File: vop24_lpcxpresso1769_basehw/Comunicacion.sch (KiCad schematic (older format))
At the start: 27 parts, among them J301 USB_B_Micro, J302 Conn_01x06_Male, J303 Conn_01x05_Male, J304 Screw_Terminal_01x02, U301 TPD4S014, U302 LTC4411, U303 LT1512

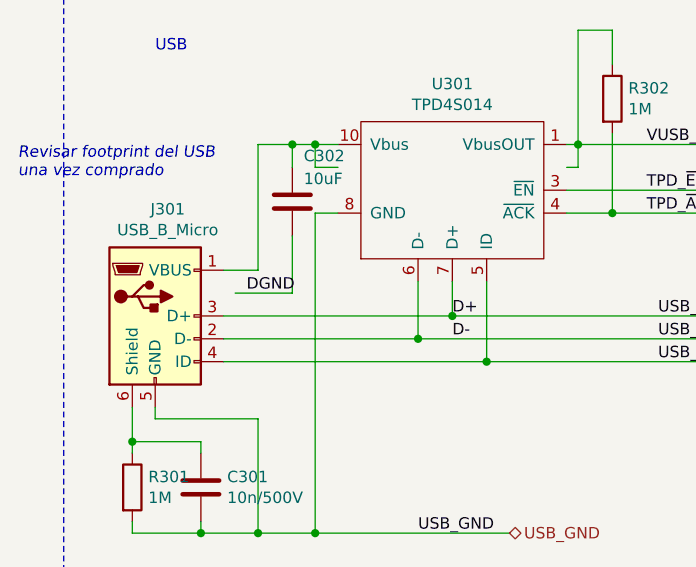
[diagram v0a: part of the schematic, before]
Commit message: PCB: ruteo e ubicacion de USB.    ESQ: cambios de etiquetas de gnd en usb
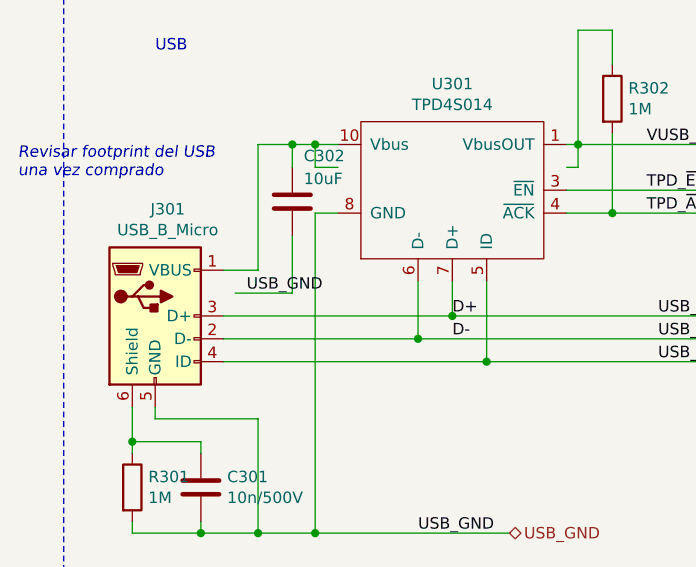
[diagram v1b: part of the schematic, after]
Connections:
- net labels removed: DGND
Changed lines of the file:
@@
 Wire Wire Line
 	1400 3800 2400 3800
-$Comp
-L vop24_lpcxpresso1769_basehw-rescue:USB_B_Micro-Connector J301
-U 1 1 5BAE3529
-P 1100 3800
-AR Path="/5BAE3529" Ref="J301"  Part="1"
-AR Path="/5B9DAB38/5BAE3529" Ref="J301"  Part="1"
-F 0 "J301" H 1155 4267 50  0000 C CNN
-F 1 "USB_B_Micro" H 1155 4176 50  0000 C CNN
-F 2 "Connector_USB:USB_Mini-B_Lumberg_2486_01_Horizontal" H 1250 3750 50  0001 C CNN
-F 3 "~" H 1250 3750 50  0001 C CNN
-	1    1100 3800
-	1    0    0    -1
-$EndComp
 Wire Wire Line
 	1400 4000 2550 4000
@@
 Wire Wire Line
 	1700 3450 1700 3700
-Text Label 1500 3700 0    50   ~ 0
-DGND
 Text Notes 500  3200 0    50   Italic 0
 Revisar footprint del USB \nuna vez comprado
@@
 Wire Wire Line
 	2950 3150 2950 3050
+$Comp
+L vop24_lpcxpresso1769_basehw-rescue:USB_B_Micro-Connector J301
+U 1 1 5BAE3529
+P 1100 3800
+AR Path="/5BAE3529" Ref="J301"  Part="1"
+AR Path="/5B9DAB38/5BAE3529" Ref="J301"  Part="1"
+F 0 "J301" H 1155 4267 50  0000 C CNN
+F 1 "USB_B_Micro" H 1155 4176 50  0000 C CNN
+F 2 "Connector_USB:USB_Mini-B_Lumberg_2486_01_Horizontal" H 1250 3750 50  0001 C CNN
+F 3 "~" H 1250 3750 50  0001 C CNN
+	1    1100 3800
+	1    0    0    -1
+$EndComp
+Text Label 1500 3700 0    50   ~ 0
+USB_GND
 $EndSCHEMATC

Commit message: ESQ: modificaciones grandes sobre correcciones del trabajo
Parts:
- removed J302: Conn_01x06_Male, Connector_PinSocket_2.54mm:PinSocket_1x06_P2.54mm_Vertical, symbol vop24_lpcxpresso1769_basehw-rescue:Conn_01x06_Male-Connector
- removed J303: Conn_01x05_Male, Connector_PinSocket_2.54mm:PinSocket_1x05_P2.54mm_Vertical, symbol vop24_lpcxpresso1769_basehw-rescue:Conn_01x05_Male-Connector
- renumbered J304 to J302, U302 to U301, U301 to U302
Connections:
- net labels removed: BLE_EN, BLE_GND, BLE_RXD, BLE_STATE, BLE_TXD, BLE_VCC, UU_5V, UU_GND, UU_RXD, UU_TXD, UU_VCC
- wire segments 129 -> 118
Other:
- note added: "Interfaces de comunicación externas:\n- USB\n- carga de batería\n- intercambio entre bateria y vusb\n"
- note removed: "BLE HM10"
- note removed: "Interfaces de comunicación externas:\n- USB\n- BLE\n- UART debug"
- note removed: "UART USB Debug"
- moved on the sheet: C301, C302, C303, C304, C305, C306, C307, C308, D301, D302, J301, J302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

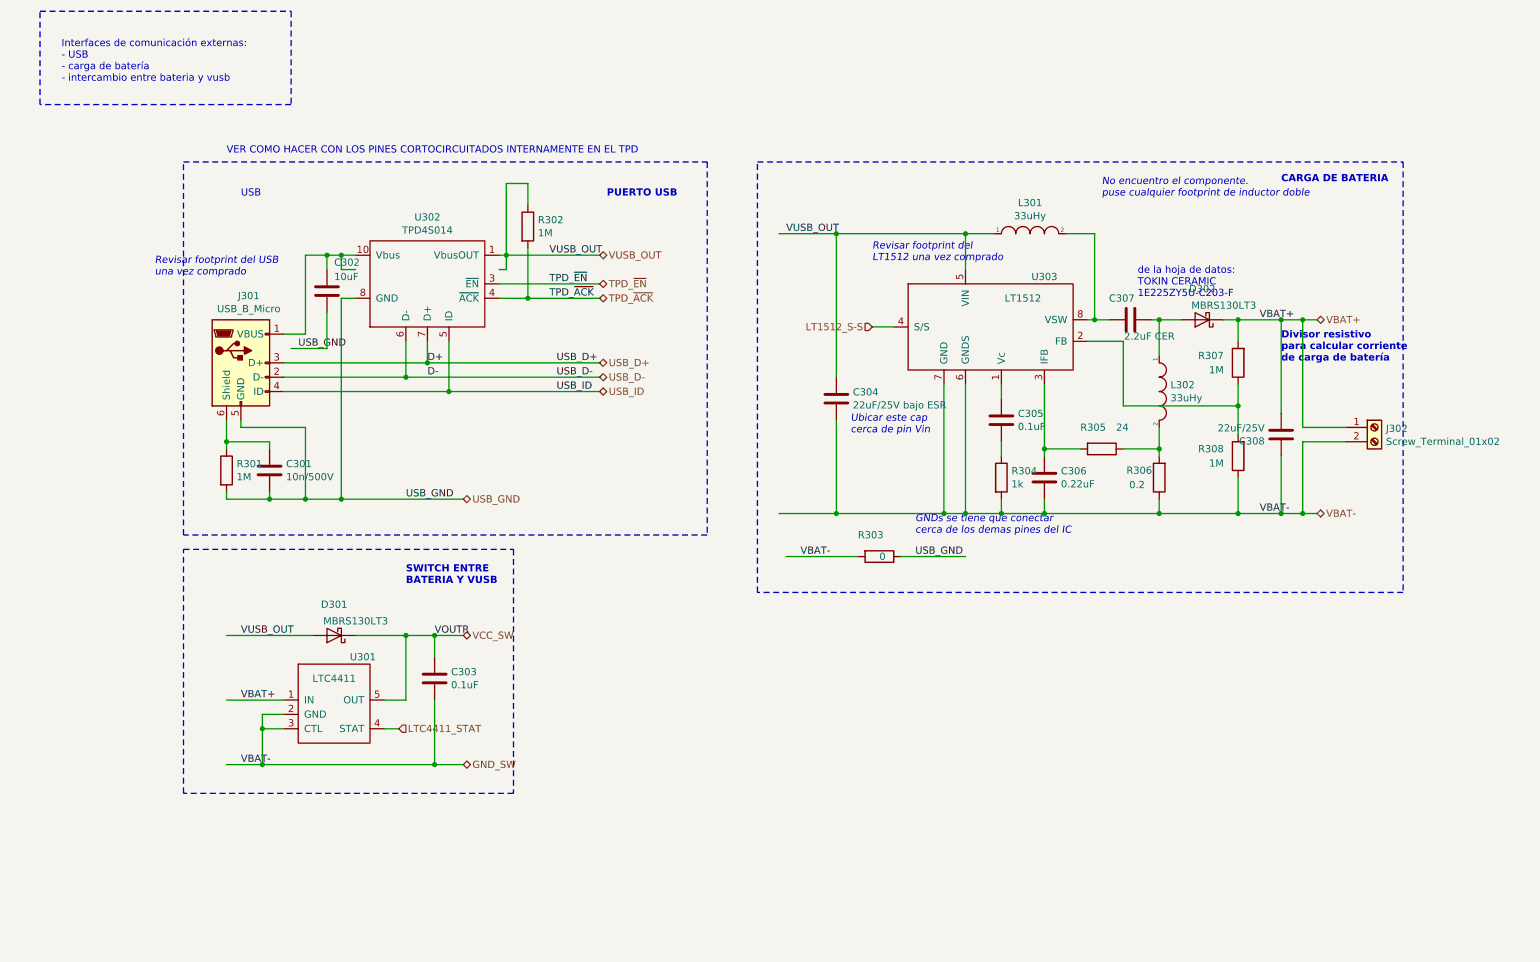
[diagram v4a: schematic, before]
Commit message: ESQ: modificaciones de etiquetas. Falta cambiar todas las conexiones de vcc
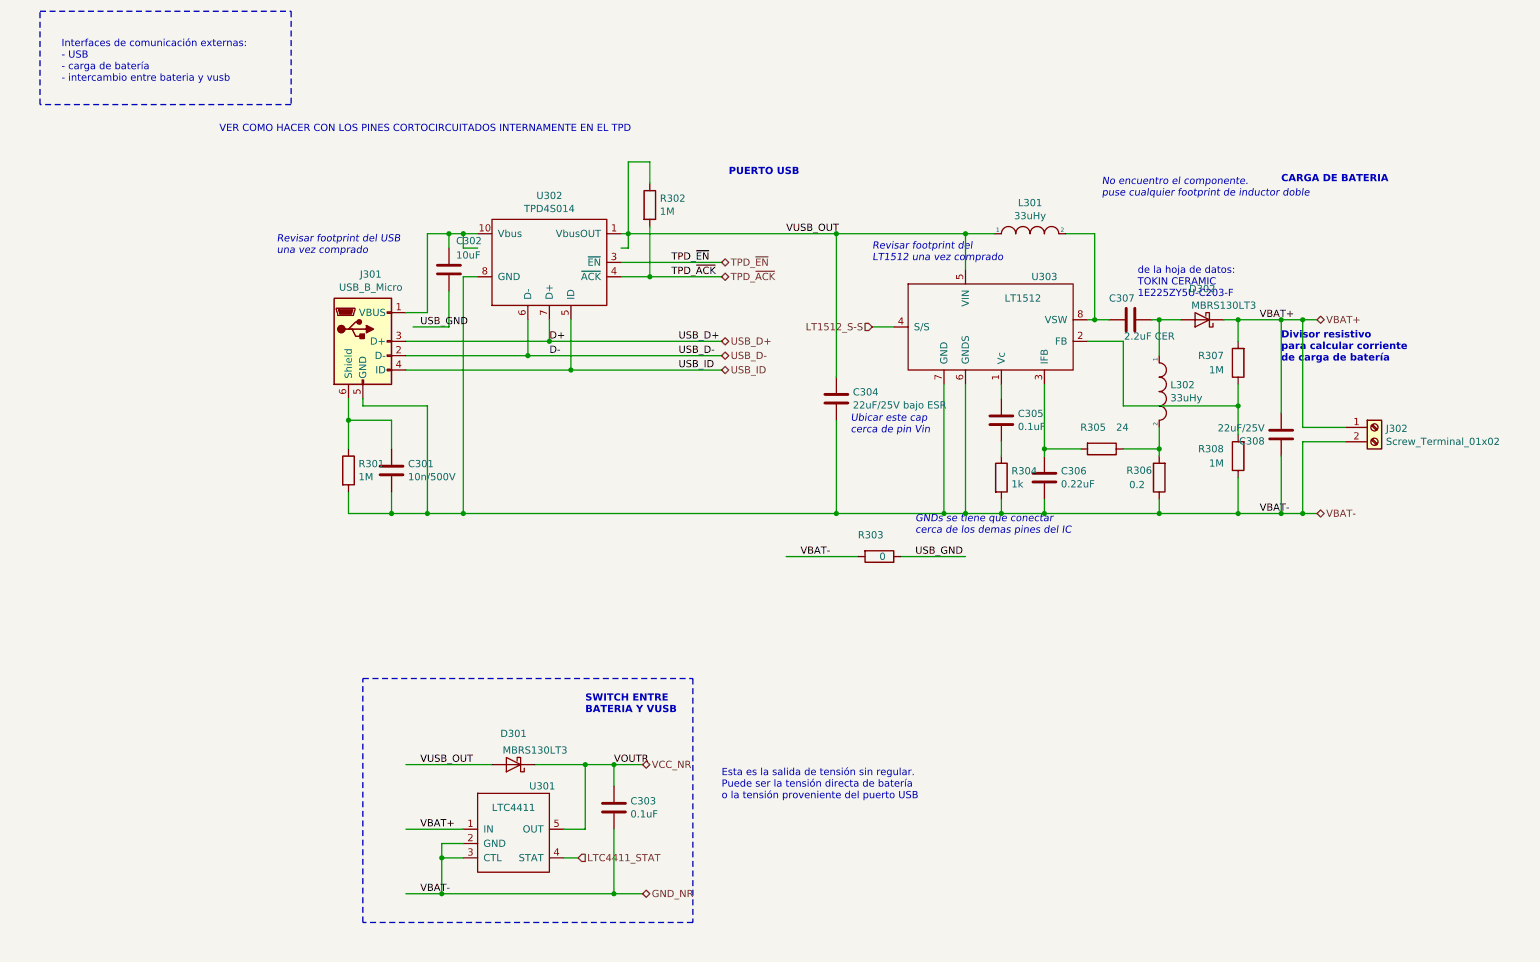
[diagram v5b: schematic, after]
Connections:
- net labels added: GND_NR, VCC_NR
- net labels removed: GND_SW, VCC_SW
- wire segments 118 -> 116
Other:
- note added: "Esta es la salida de tensión sin regular.\nPuede ser la tensión directa de batería\no la tensión proveniente del puerto USB"
- note removed: "USB"
- moved on the sheet: C301, C302, C303, D301, J301, R301, R302, U301, U302

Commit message: ESQ: cambios sobre etiquetas y simbolos de POWER
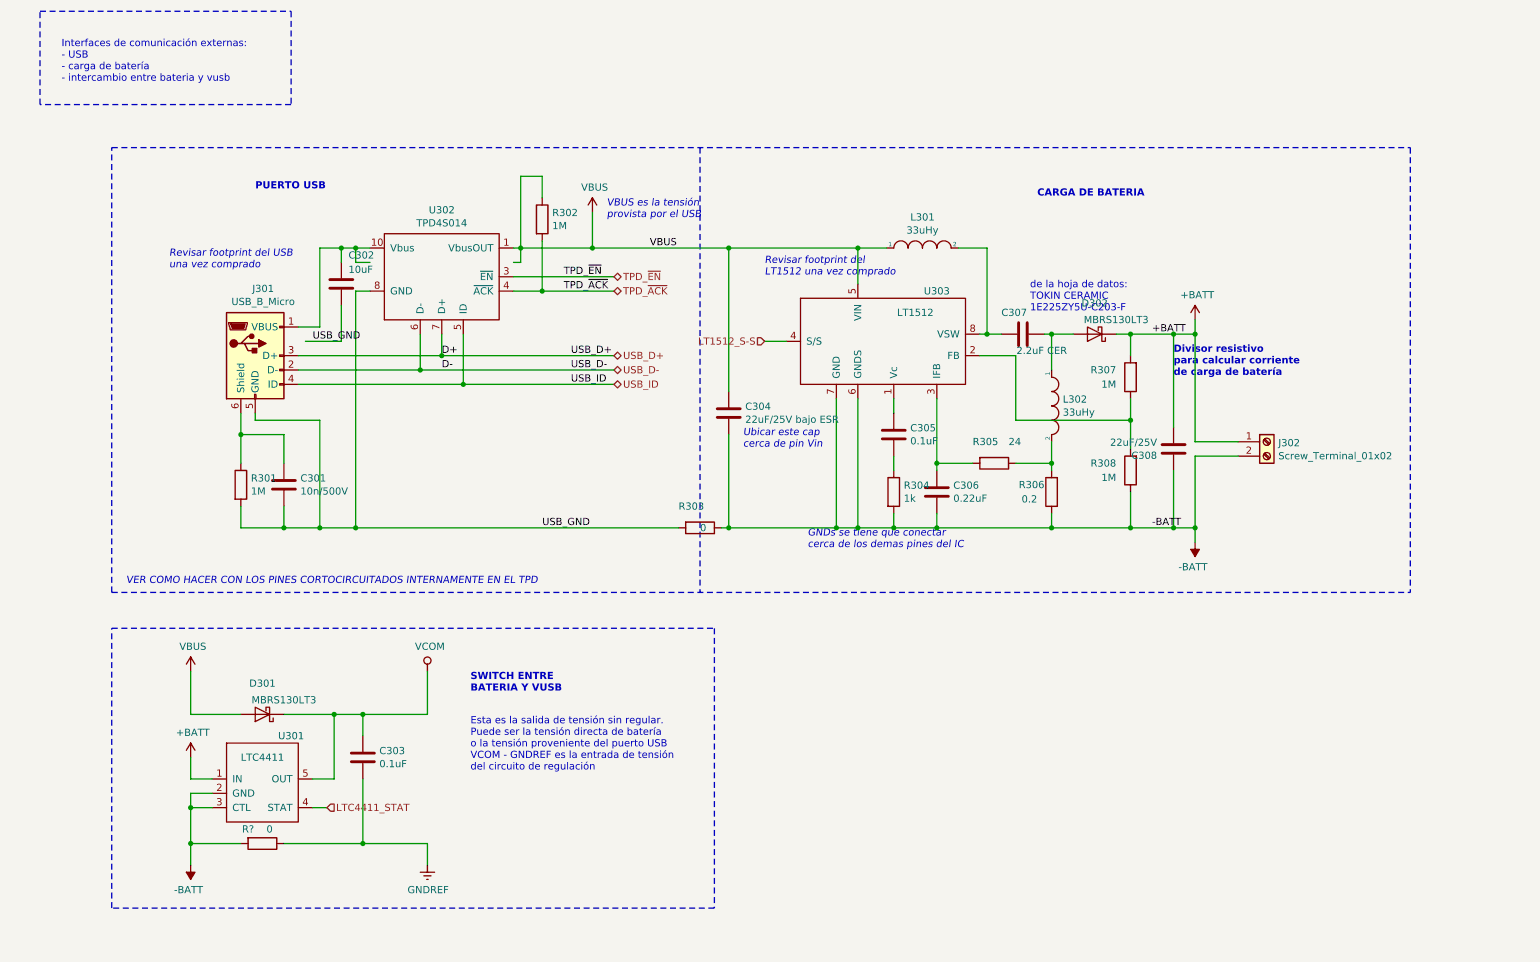
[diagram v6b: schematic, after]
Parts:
- added R?: 0, symbol Device:R
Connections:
- net labels added: +BATT, -BATT, GNDREF, VBUS, VCOM
- net labels removed: GND_NR, VBAT+, VBAT-, VCC_NR, VOUTR, VUSB_OUT
- wire segments 116 -> 122
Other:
- note added: "Esta es la salida de tensión sin regular.\nPuede ser la tensión directa de batería\no la tensión proveniente del puerto USB\nVCOM - GNDREF es la entrada de tensión\ndel circuito de regulación"
- note added: "VBUS es la tensión \nprovista por el USB"
- note removed: "Esta es la salida de tensión sin regular.\nPuede ser la tensión directa de batería\no la tensión proveniente del puerto USB"
- note removed: "No encuentro el componente.\npuse cualquier footprint de inductor doble"
- moved on the sheet: C301, C302, C303, C304, C305, C306, C307, C308, D301, D302, J301, J302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
